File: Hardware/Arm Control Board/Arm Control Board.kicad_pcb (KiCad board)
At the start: 2 copper layers, 99 parts, among them P1 Servo 1, P10 UIM240XX_Stepper_Conn, P11 Battery, P12 SyRen, P13 Raspberry Pi, P2 Shoulder Feedback, P3 Servo 2, P4 Servo 3, P5 Elbow Feedback, P6 Servo 4, P7 RS485, P8 ST_SWD_Connector, P9 Servo 5, U1 STM32F401RCT6, U2 SN75176BDR, U3 74LVCH244APW, U4 AOZ1280CI, U5 AOZ1280CI, U6 AP65552SP-13, U7 AP65552SP-13, U8 AP65552SP-13, U9 AP65552SP-13, X1 24MHz

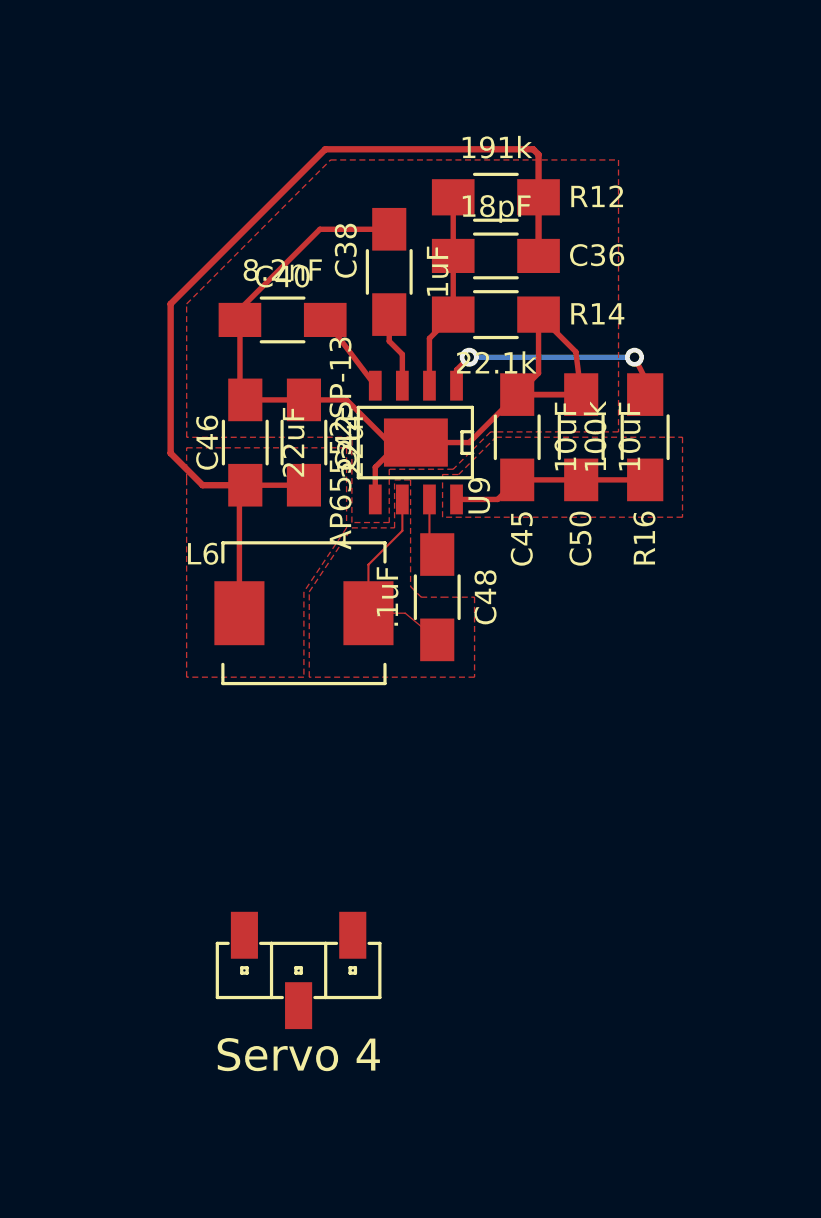
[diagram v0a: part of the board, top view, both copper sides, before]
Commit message: adding vias so the ground doesn't com*plane*
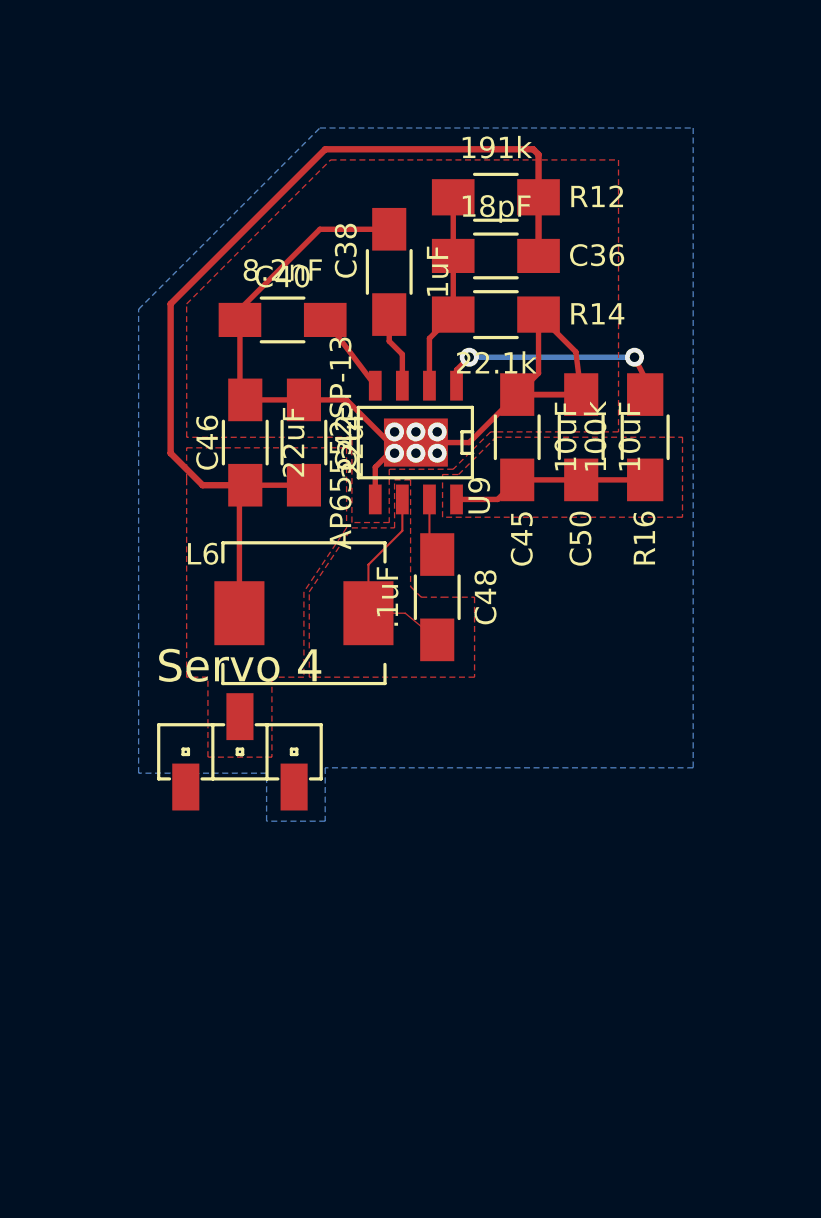
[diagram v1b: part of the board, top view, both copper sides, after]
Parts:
- moved P6 10.6 mm to (100.2, 153.8), turned to 180 degrees
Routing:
- net GND: track 147.0 -> 158.6 mm, vias 0 -> 6
- added copper zone on B.Cu, net GND
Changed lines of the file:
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@@
   (general
     (links 237)
-    (no_connects 143)
-    (area -85.462333 -13.479 352.410859 242.079001)
+    (no_connects 142)
+    (area 10.449999 10.449999 11.050001 10.550001)
     (thickness 1.6)
     (drawings 1)
-    (tracks 223)
+    (tracks 242)
     (zones 0)
     (modules 99)
@@
     (pad_to_mask_clearance 0)
     (aux_axis_origin 0 0)
-    (visible_elements 7FFEFF7F)
+    (visible_elements 7FFEFFFF)
     (pcbplotparams
       (layerselection 0x00030_80000001)
@@
   )
   (module MAVRIC_footprints:1x3_SMD_header (layer F.Cu)
-    (at 103 164)
-    (fp_text reference P6 (at 0 -4) (layer F.SilkS) hide
+    (at 100.25 153.75 180)
+    (fp_text reference P6 (at 0 -4 180) (layer F.SilkS) hide
       (effects (font (size 1.5 1.5) (thickness 0.15)))
     )
-    (fp_text value "Servo 4" (at 0 4) (layer F.SilkS)
+    (fp_text value "Servo 4" (at 0 4 180) (layer F.SilkS)
       (effects (font (size 1.5 1.5) (thickness 0.15)))
     )
@@
     (fp_line (start -2.413 0.127) (end -2.413 -0.127) (layer F.SilkS) (width 0.15))
     (fp_line (start -2.413 -0.127) (end -2.667 -0.127) (layer F.SilkS) (width 0.15))
-    (pad 2 smd rect (at 0 1.65) (size 1.27 2.2) (layers F.Cu F.Paste F.Mask)
+    (pad 2 smd rect (at 0 1.65 180) (size 1.27 2.2) (layers F.Cu F.Paste F.Mask)
       (net 27 "/7.4V Regulators/REG4+7V4"))
-    (pad 1 smd rect (at -2.54 -1.65) (size 1.27 2.2) (layers F.Cu F.Paste F.Mask)
+    (pad 1 smd rect (at -2.54 -1.65 180) (size 1.27 2.2) (layers F.Cu F.Paste F.Mask)
       (net 2 GND))
-    (pad 3 smd rect (at 2.54 -1.65) (size 1.27 2.2) (layers F.Cu F.Paste F.Mask)
+    (pad 3 smd rect (at 2.54 -1.65 180) (size 1.27 2.2) (layers F.Cu F.Paste F.Mask)
       (net 89 /Servo4_PWM))
   )
@@
   )
   (gr_line (start 10.5 10.5) (end 11 10.5) (angle 90) (layer Edge.Cuts) (width 0.1))
-  (segment (start 106.595 141.917) (end 106.595 140.405) (width 0.254) (layer F.Cu) (net 2))
-  (segment (start 106.595 140.405) (end 107.75 139.25) (width 0.254) (layer F.Cu) (net 2))
-  (segment (start 107.75 139.25) (end 108.5 139.25) (width 0.254) (layer F.Cu) (net 2))
+  (segment (start 100.5 137.25) (end 105.25 137.25) (width 0.254) (layer F.Cu) (net 2) (status 10))
+  (segment (start 105.25 137.25) (end 107.25 139.25) (width 0.254) (layer F.Cu) (net 2) (status 20))
+  (segment (start 109.5 139.75) (end 108.5 139.75) (width 0.1) (layer B.Cu) (net 2))
+  (via (at 109.5 139.75) (size 0.889) (layers F.Cu B.Cu) (net 2))
+  (segment (start 108.5 139.75) (end 107.5 139.75) (width 0.1) (layer B.Cu) (net 2))
+  (via (at 107.5 139.75) (size 0.889) (layers F.Cu B.Cu) (net 2))
+  (segment (start 108.5 139.75) (end 107.5 139.75) (width 0.1) (layer B.Cu) (net 2))
+  (segment (start 107.5 139.75) (end 107.5 138.75) (width 0.1) (layer B.Cu) (net 2))
+  (segment (start 107.5 138.75) (end 108.5 138.75) (width 0.1) (layer B.Cu) (net 2))
+  (segment (start 108.5 138.75) (end 109.5 138.75) (width 0.1) (layer B.Cu) (net 2))
+  (segment (start 109.5 138.75) (end 109.5 139.75) (width 0.1) (layer B.Cu) (net 2))
+  (segment (start 108.5 139.25) (end 108.5 139.75) (width 0.1) (layer F.Cu) (net 2))
+  (via (at 108.5 139.75) (size 0.889) (layers F.Cu B.Cu) (net 2))
+  (segment (start 108.5 139.25) (end 108.25 139.25) (width 0.1) (layer F.Cu) (net 2))
+  (segment (start 108.25 139.25) (end 107.5 138.75) (width 0.1) (layer F.Cu) (net 2))
+  (segment (start 109.5 138.75) (end 109.5 139.75) (width 0.1) (layer B.Cu) (net 2))
+  (via (at 109.5 138.75) (size 0.889) (layers F.Cu B.Cu) (net 2))
+  (segment (start 108.5 138.75) (end 109.5 138.75) (width 0.1) (layer F.Cu) (net 2))
+  (via (at 108.5 138.75) (size 0.889) (layers F.Cu B.Cu) (net 2))
+  (segment (start 107.5 138.75) (end 108.5 138.75) (width 0.1) (layer B.Cu) (net 2))
+  (via (at 107.5 138.75) (size 0.889) (layers F.Cu B.Cu) (net 2))
+  (segment (start 107.75 139.25) (end 108.5 139.25) (width 0.254) (layer F.Cu) (net 2) (status 30))
+  (segment (start 106.595 141.917) (end 106.595 140.405) (width 0.254) (layer F.Cu) (net 2) (status 10))
+  (segment (start 106.595 140.405) (end 107.75 139.25) (width 0.254) (layer F.Cu) (net 2) (status 20))
   (segment (start 100.25 133.5) (end 100.25 133) (width 0.254) (layer F.Cu) (net 2) (status 10))
   (segment (start 104 129.25) (end 107.25 129.25) (width 0.254) (layer F.Cu) (net 2))
@@
   (segment (start 100.25 133.5) (end 100.25 137) (width 0.254) (layer F.Cu) (net 2) (status 10))
   (segment (start 100.25 137) (end 100.5 137.25) (width 0.254) (layer F.Cu) (net 2) (status 30))
-  (segment (start 100.5 137.25) (end 105.25 137.25) (width 0.254) (layer F.Cu) (net 2) (status 10))
-  (segment (start 105.25 137.25) (end 107.25 139.25) (width 0.254) (layer F.Cu) (net 2))
-  (segment (start 107.25 139.25) (end 111 139.25) (width 0.254) (layer F.Cu) (net 2))
+  (segment (start 107.25 139.25) (end 111 139.25) (width 0.254) (layer F.Cu) (net 2) (status 10))
   (segment (start 111 139.25) (end 113.25 137) (width 0.254) (layer F.Cu) (net 2))
   (segment (start 113.25 137) (end 116.25 137) (width 0.254) (layer F.Cu) (net 2) (status 20))
@@
   (segment (start 116.25 141) (end 113.25 141) (width 0.254) (layer F.Cu) (net 12) (status 10))
   (segment (start 113.25 141) (end 112.333 141.917) (width 0.254) (layer F.Cu) (net 12))
-  (segment (start 112.333 141.917) (end 110.405 141.917) (width 0.254) (layer F.Cu) (net 12))
+  (segment (start 112.333 141.917) (end 110.405 141.917) (width 0.254) (layer F.Cu) (net 12) (status 20))
   (segment (start 232.25 120.25) (end 232.25 121) (width 0.254) (layer F.Cu) (net 12))
   (segment (start 232.25 121) (end 233 121.75) (width 0.254) (layer F.Cu) (net 12))
@@
   (segment (start 110.25 130.5) (end 110.25 133.25) (width 0.254) (layer F.Cu) (net 28))
   (segment (start 110.25 133.25) (end 109.135 134.365) (width 0.254) (layer F.Cu) (net 28))
-  (segment (start 109.135 134.365) (end 109.135 136.583) (width 0.254) (layer F.Cu) (net 28))
+  (segment (start 109.135 134.365) (end 109.135 136.583) (width 0.254) (layer F.Cu) (net 28) (status 20))
   (segment (start 184.385 135.365) (end 180.25 139.5) (width 0.254) (layer F.Cu) (net 29))
   (segment (start 184.385 133.167) (end 184.385 135.365) (width 0.254) (layer F.Cu) (net 29))
   (segment (start 107.25 133.25) (end 107.25 134.5) (width 0.254) (layer F.Cu) (net 30))
-  (segment (start 107.865 135.115) (end 107.865 136.583) (width 0.254) (layer F.Cu) (net 30))
+  (segment (start 107.865 135.115) (end 107.865 136.583) (width 0.254) (layer F.Cu) (net 30) (status 20))
   (segment (start 107.25 134.5) (end 107.865 135.115) (width 0.254) (layer F.Cu) (net 30))
   (segment (start 185.655 136.595) (end 180.25 142) (width 0.254) (layer F.Cu) (net 31))
   (segment (start 185.655 133.167) (end 185.655 136.595) (width 0.254) (layer F.Cu) (net 31))
   (segment (start 104.25 133.5) (end 104.262 133.5) (width 0.254) (layer F.Cu) (net 32) (status 30))
-  (segment (start 104.262 133.5) (end 106.595 136.583) (width 0.254) (layer F.Cu) (net 32) (status 10))
+  (segment (start 104.262 133.5) (end 106.595 136.583) (width 0.254) (layer F.Cu) (net 32) (status 20))
   (segment (start 183.115 126.365) (end 183.115 127.833) (width 0.254) (layer F.Cu) (net 33))
   (segment (start 181.75 125) (end 183.115 126.365) (width 0.254) (layer F.Cu) (net 33))
@@
   (segment (start 184.385 125.865) (end 184.385 127.833) (width 0.254) (layer F.Cu) (net 34))
   (segment (start 184.72486 123) (end 184.72486 125.52514) (width 0.254) (layer F.Cu) (net 34))
-  (segment (start 109.135 141.917) (end 109.135 144.135) (width 0.1) (layer F.Cu) (net 35))
+  (segment (start 109.135 141.917) (end 109.135 144.135) (width 0.1) (layer F.Cu) (net 35) (status 10))
   (segment (start 109.135 144.135) (end 109.5 144.5) (width 0.1) (layer F.Cu) (net 35))
   (segment (start 109.385 144.385) (end 109.5 144.5) (width 0.254) (layer F.Cu) (net 35) (status 30))
   (segment (start 106.27514 147.25) (end 108 147.25) (width 0.008) (layer F.Cu) (net 36) (status 10))
   (segment (start 108 147.25) (end 109.5 148.5) (width 0.008) (layer F.Cu) (net 36) (status 20))
-  (segment (start 107.865 141.917) (end 107.865 143.385) (width 0.1) (layer F.Cu) (net 36))
+  (segment (start 107.865 141.917) (end 107.865 143.385) (width 0.1) (layer F.Cu) (net 36) (status 10))
   (segment (start 107.865 143.385) (end 106.27514 144.97486) (width 0.1) (layer F.Cu) (net 36))
   (segment (start 106.27514 144.97486) (end 106.27514 147.25) (width 0.1) (layer F.Cu) (net 36) (status 20))
@@
   (via (at 111 135.25) (size 0.889) (layers F.Cu B.Cu) (net 42))
   (segment (start 110.405 135.845) (end 111 135.25) (width 0.254) (layer F.Cu) (net 42))
-  (segment (start 110.405 136.583) (end 110.405 135.845) (width 0.254) (layer F.Cu) (net 42))
+  (segment (start 110.405 136.583) (end 110.405 135.845) (width 0.254) (layer F.Cu) (net 42) (status 10))
   (segment (start 118.75 135.25) (end 119.25 136.25) (width 0.254) (layer F.Cu) (net 42) (status 20))
   (via (at 118.75 135.25) (size 0.889) (layers F.Cu B.Cu) (net 42))
@@
     (polygon
       (pts
-        (xy 105.25 143.25) (xy 103.25 146.25) (xy 103.25 150.25) (xy 97.75 150.25) (xy 97.75 143.5)
+        (xy 105.25 143.25) (xy 103.25 146.25) (xy 103.25 150.25) (xy 101.75 150.25) (xy 101.75 154)
+        (xy 98.75 154) (xy 98.75 152.5) (xy 98.75 150.25) (xy 97.75 150.25) (xy 97.75 143.5)
         (xy 97.75 141) (xy 97.75 139.496) (xy 105.25 139.496)
       )
@@
       )
     )
+  )
+  (zone (net 2) (net_name GND) (layer B.Cu) (hatch edge 0.508)
+    (connect_pads (clearance 0.2))
+    (min_thickness 0.2)
+    (fill yes (arc_segments 16) (thermal_gap 0.508) (thermal_bridge_width 0.508))
+    (polygon
+      (pts
+        (xy 104 124.5) (xy 121.5 124.5) (xy 121.5 154.5) (xy 104.25 154.5) (xy 104.25 157)
+        (xy 101.5 157) (xy 101.5 154.75) (xy 95.5 154.75) (xy 95.5 133) (xy 104 124.5)
+      )
+    )

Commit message: more vias but to be honest the situation is a mess
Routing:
- net GND: track 158.6 -> 173.8 mm, vias 6 -> 21
- net (no net): track 0.00 -> 1.00 mm, vias 0 -> 2

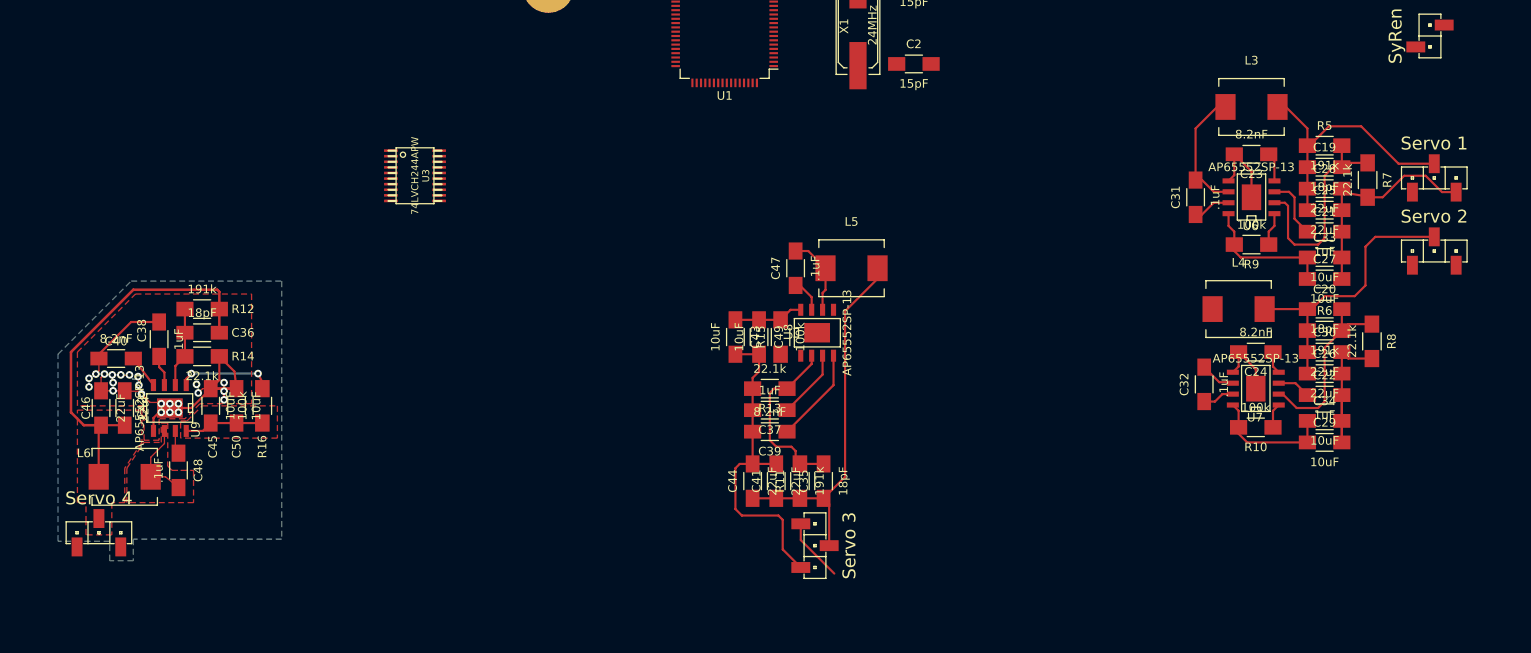
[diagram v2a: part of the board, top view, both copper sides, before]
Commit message: Added current sensing to reg1-4, updated STMCube
Only high current servo outputs have current sensing. STMCube was not up
to date with pin assignments. Issues: #18 #15
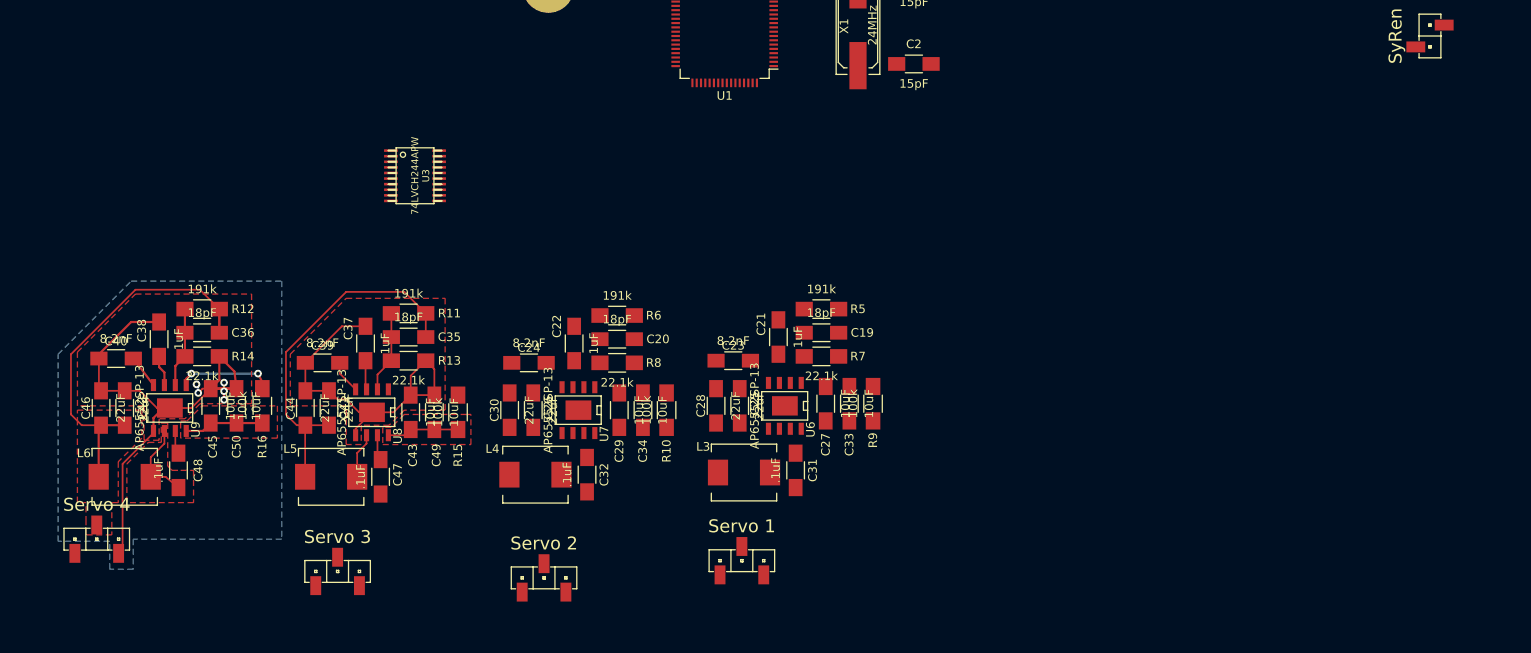
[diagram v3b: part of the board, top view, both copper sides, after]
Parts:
- moved P3 110.3 mm to (152.0, 159.0)
- moved C30 95.0 mm to (148.0, 139.5), turned to 90 degrees
- moved C26 92.1 mm to (150.8, 139.5), turned to 90 degrees
- moved P1 92.0 mm to (175.0, 157.0)
- moved R8 87.8 mm to (160.5, 134.0), turned to 0 degrees
- moved C22 87.5 mm to (155.5, 131.8), turned to 90 degrees
- moved C24 84.5 mm to (150.2, 134.0)
- moved L4 84.0 mm to (151.0, 147.0), turned to 180 degrees
- moved C20 82.3 mm to (160.5, 131.2), turned to 180 degrees
- moved R6 82.3 mm to (160.5, 128.5), turned to 180 degrees
- moved C29 82.1 mm to (160.8, 139.5), turned to 90 degrees
- moved C34 79.3 mm to (163.5, 139.5), turned to 90 degrees
- moved U7 78.8 mm to (156.0, 139.5), turned to 180 degrees
- moved C28 75.1 mm to (172.0, 139.0), turned to 90 degrees
- moved L3 72.7 mm to (175.2, 146.8), turned to 180 degrees
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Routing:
- net GND: track 173.8 -> 110.6 mm, vias 21 -> 5
- net /7.4V Regulators/REG2+7V4: track 33.3 -> 0.00 mm
- net /7.4V Regulators/REG1+7V4: track 31.5 -> 0.00 mm
- net +12V: track 47.8 -> 17.6 mm
- net Net-(C19-Pad2): track 26.2 -> 0.00 mm
- net Net-(C20-Pad2): track 21.7 -> 0.00 mm
- net Net-(C31-Pad2): track 14.9 -> 0.00 mm
- net Net-(C35-Pad2): track 20.7 -> 9.50 mm
- net Net-(C21-Pad1): track 7.72 -> 0.00 mm
- net /Servo3_PWM: track 7.41 -> 0.00 mm
- net Net-(C39-Pad1): track 11.1 -> 3.85 mm
- net Net-(C37-Pad1): track 8.05 -> 3.38 mm
- net Net-(C31-Pad1): track 4.40 -> 0.00 mm
- net Net-(C32-Pad2): track 4.11 -> 0.00 mm
- net Net-(C47-Pad2): track 9.28 -> 5.28 mm
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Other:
- net class 7v4 Power removed
- net class Default: clearance 0.008 -> 0.2032; trace_width 0.1 -> 0.2032
- rule trace_clearance: 0.008 -> 0.2032
- rule trace_min: 0.008 -> 0.2032
